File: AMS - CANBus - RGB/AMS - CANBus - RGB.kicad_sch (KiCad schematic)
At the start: 16 parts, among them J1 Power_And_CAN, J2 Power_And_CAN, J6 Screw_Terminal_01x02, Q1 IRF9Z34NPBF, U1 3568, U5 3568

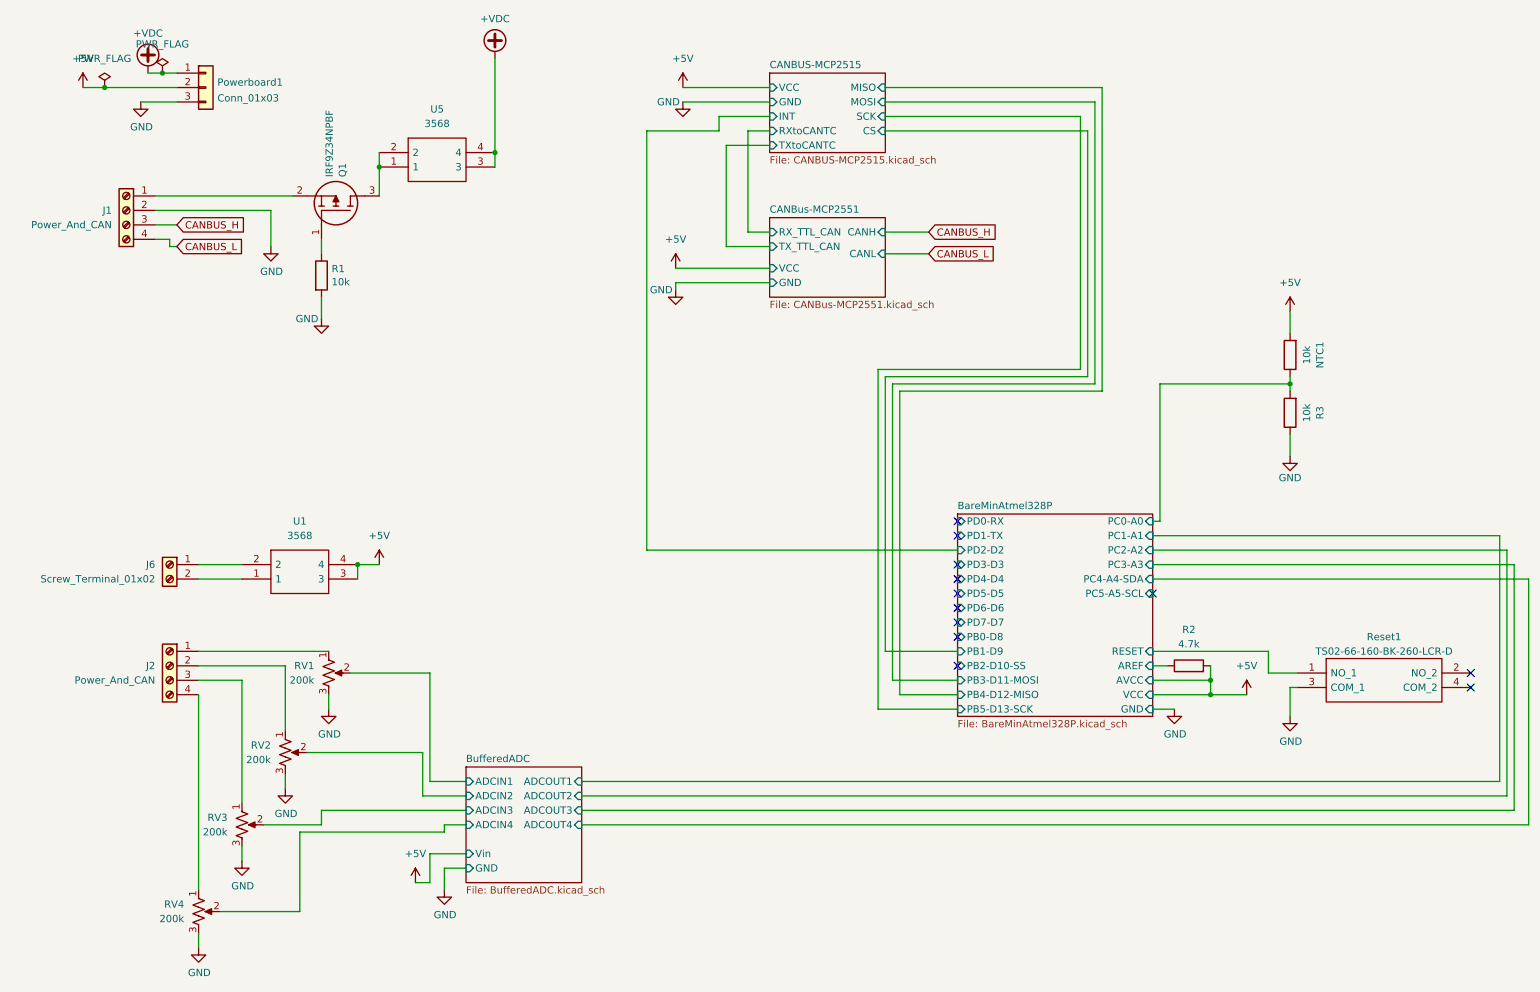
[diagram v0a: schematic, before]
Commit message: removal of the Input stuff from the Voltage Board this was copied from
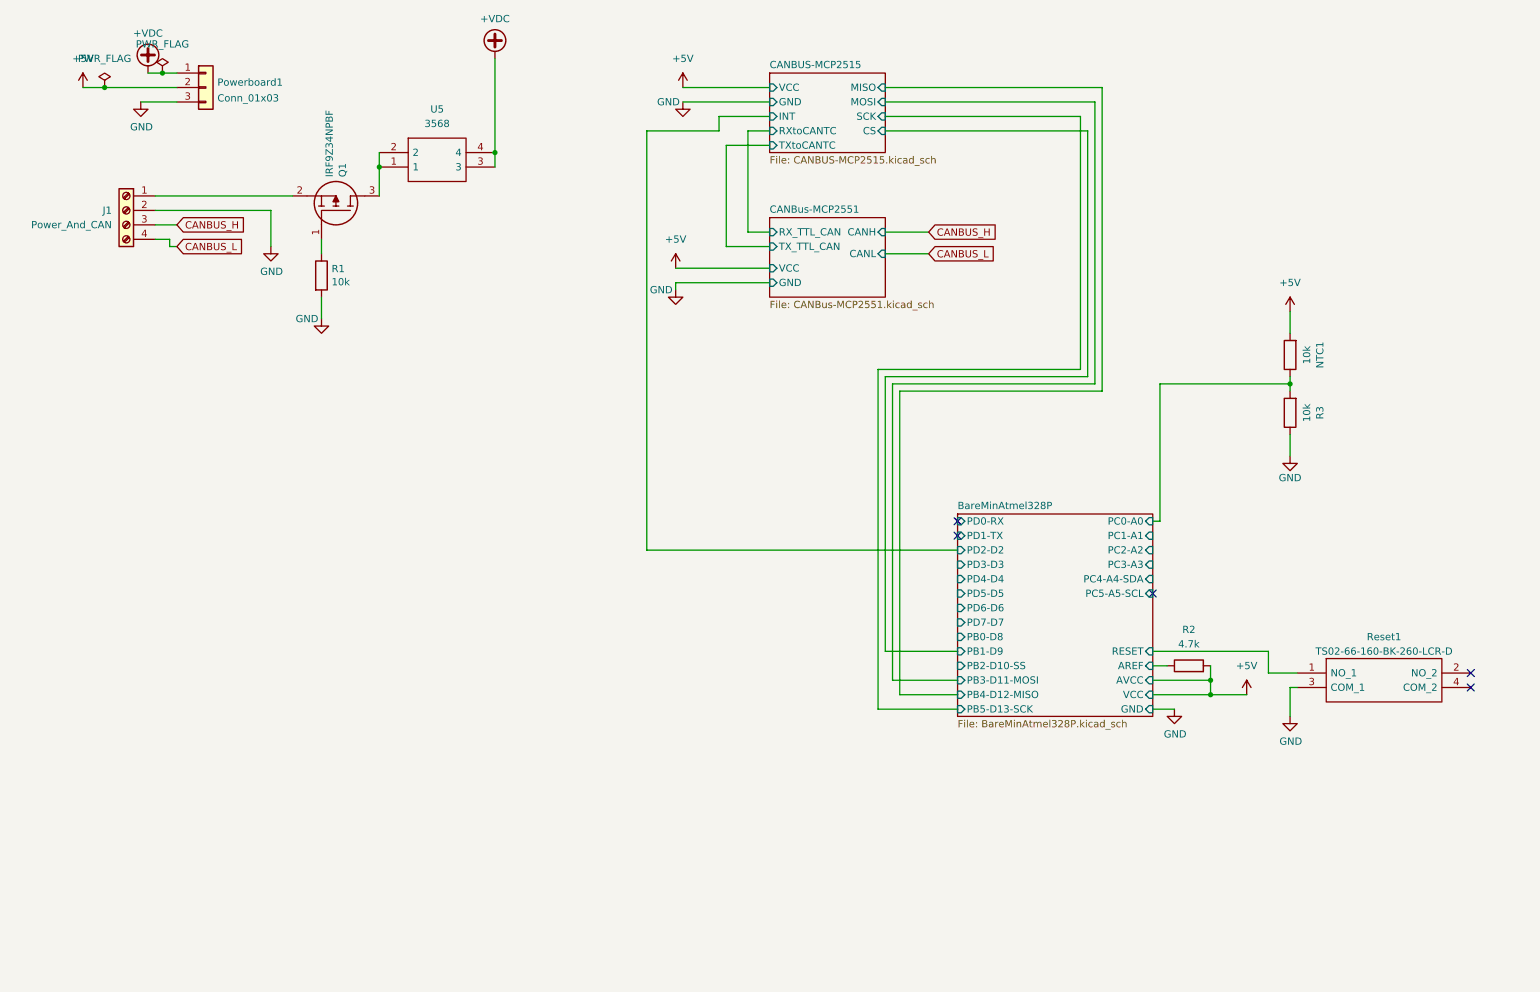
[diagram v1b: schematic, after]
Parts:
- removed J2: Power_And_CAN, TerminalBlock_Phoenix:TerminalBlock_Phoenix_MPT-0,5-4-2.54_1x04_P2.54mm_Horizontal, symbol Connector:Screw_Terminal_01x04
- removed J6: Screw_Terminal_01x02, TerminalBlock_Phoenix:TerminalBlock_Phoenix_MPT-0,5-2-2.54_1x02_P2.54mm_Horizontal, symbol Connector:Screw_Terminal_01x02
- removed RV1, RV2, RV3, RV4: 200k, Potentiometer_THT:Potentiometer_Bourns_3296W_Vertical, symbol Device:R_Potentiometer_US
- removed U1: 3568, 3568, symbol SamacSys_Parts:3568
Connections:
- no-connect marks 12 -> 5
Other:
- removed sheet BufferedADC
